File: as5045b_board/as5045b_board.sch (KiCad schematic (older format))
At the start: 10 parts

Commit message: QS
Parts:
- removed C?: 10uF, Capacitor_SMD:C_0603_1608Metric, symbol Device:C_Small
- removed C?: 0.1uF, Capacitor_SMD:C_0402_1005Metric, symbol Device:C_Small
- removed R? (x2): 10K, Resistor_SMD:R_0402_1005Metric, symbol Device:R_Small
- removed U? (x2): AS5045B, Package_SO:SSOP-16_5.3x6.2mm_P0.65mm, symbol Sensor_Magnetic:AS5045B
- added C1: 0.1uF, Capacitor_SMD:C_0402_1005Metric, symbol Device:C_Small
- added C3: 10uF, Capacitor_SMD:C_0603_1608Metric, symbol Device:C_Small
- added R1, R3, R5, R7: 2K2, Resistor_SMD:R_0402_1005Metric, symbol Device:R_Small
- added R10, R11, R12, R9: 10K, Resistor_SMD:R_0402_1005Metric, symbol Device:R_Small
- added R2, R4, R6, R8: 3K3, Resistor_SMD:R_0402_1005Metric, symbol Device:R_Small
- added U1, U2: AS5304, Package_SO:TSSOP-20_4.4x6.5mm_P0.65mm, symbol ams:AS5304
- gave numbers to parts that had none: 4
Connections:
- net labels added: +5V
- net labels removed: +3V3
- wire segments 30 -> 62
- no-connect marks 14 -> 0
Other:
- moved on the sheet: C2, C4, J1, J2

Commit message: Finished encoders, added XSHUT pullups
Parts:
- J1, J2: footprint Connector_PinHeader_1.00mm:PinHeader_1x04_P1.00mm_Vertical_SMD_Pin1Left -> connector_brd2brd:01x04_1.0x0.5mm_SMD
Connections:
- wire segments 62 -> 67
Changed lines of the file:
@@
 F 0 "J1" H 3700 3450 50  0000 C CNN
 F 1 "Conn_01x04" H 3700 3350 50  0000 C CNN
-F 2 "Connector_PinHeader_1.00mm:PinHeader_1x04_P1.00mm_Vertical_SMD_Pin1Left" H 3700 3100 50  0001 C CNN
+F 2 "connector_brd2brd:01x04_1.0x0.5mm_SMD" H 3700 3100 50  0001 C CNN
 F 3 "~" H 3700 3100 50  0001 C CNN
 	1    3700 3100
@@
 F 0 "J2" H 3700 4750 50  0000 C CNN
 F 1 "Conn_01x04" H 3700 4650 50  0000 C CNN
-F 2 "Connector_PinHeader_1.00mm:PinHeader_1x04_P1.00mm_Vertical_SMD_Pin1Left" H 3700 4400 50  0001 C CNN
+F 2 "connector_brd2brd:01x04_1.0x0.5mm_SMD" H 3700 4400 50  0001 C CNN
 F 3 "~" H 3700 4400 50  0001 C CNN
 	1    3700 4400
@@
 	1    0    0    -1
 $EndComp
-Connection ~ 5150 3300
 $Comp
 L Device:R_Small R9
@@
 	1    0    0    -1
 $EndComp
-Connection ~ 4900 3200
 $Comp
 L Device:R_Small R10
@@
 	1    0    0    -1
 $EndComp
-Connection ~ 4900 4500
 $Comp
 L Device:R_Small R12
@@
 	1    0    0    -1
 $EndComp
-Connection ~ 5150 4600
 $Comp
 L power:+5V #PWR0111
@@
 	3950 4600 3900 4600
 Connection ~ 4050 4800
-Wire Wire Line
-	4050 4600 5150 4600
-Wire Wire Line
-	4350 4500 4900 4500
 $Comp
 L power:GND #PWR0113
@@
 Connection ~ 4350 3400
 Wire Wire Line
-	4350 3200 4900 3200
-Wire Wire Line
-	4050 3300 5150 3300
-Wire Wire Line
 	3900 3100 4800 3100
 Wire Wire Line
@@
 	1    0    0    -1
 $EndComp
+Connection ~ 5150 3300
+Wire Wire Line
+	4050 3300 5150 3300
+Connection ~ 4900 3200
+Wire Wire Line
+	4350 3200 4900 3200
+Wire Wire Line
+	5150 4600 4550 4600
+Wire Wire Line
+	4550 4600 4550 4500
+Wire Wire Line
+	4550 4500 4350 4500
+Connection ~ 5150 4600
+Wire Wire Line
+	4650 4500 4650 4450
+Wire Wire Line
+	4650 4450 4050 4450
+Wire Wire Line
+	4050 4450 4050 4600
+Wire Wire Line
+	4650 4500 4900 4500
+Connection ~ 4900 4500
 $EndSCHEMATC

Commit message: Czyszczenie
Usunięto linie 5V oraz 2V8. Poprawiono symbol dla diody RGB
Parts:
- R10, R11, R12, R9: value 10K -> DNP
- U1, U2: symbol ams:AS5304 -> as5045b_board-rescue:AS5304-ams
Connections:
- wire segments 67 -> 72
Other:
- note added: "Note:\nPin 20 of AS5304 is connected manually\nto GND on PBC Layout Editor"
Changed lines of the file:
@@
 $EndComp
 $Comp
-L ams:AS5304 U1
+L as5045b_board-rescue:AS5304-ams U1
 U 1 1 5E66F302
 P 5750 3250
@@
 $EndComp
 $Comp
-L ams:AS5304 U2
+L as5045b_board-rescue:AS5304-ams U2
 U 1 1 5E66FC47
 P 5750 4550
@@
 P 5150 3200
 F 0 "R11" H 5209 3246 50  0000 L CNN
-F 1 "10K" H 5209 3155 50  0000 L CNN
+F 1 "DNP" H 5209 3155 50  0000 L CNN
 F 2 "Resistor_SMD:R_0402_1005Metric" H 5150 3200 50  0001 C CNN
 F 3 "~" H 5150 3200 50  0001 C CNN
@@
 P 4900 3100
 F 0 "R9" H 4959 3146 50  0000 L CNN
-F 1 "10K" H 4959 3055 50  0000 L CNN
+F 1 "DNP" H 4959 3055 50  0000 L CNN
 F 2 "Resistor_SMD:R_0402_1005Metric" H 4900 3100 50  0001 C CNN
 F 3 "~" H 4900 3100 50  0001 C CNN
@@
 P 4900 4400
 F 0 "R10" H 4959 4446 50  0000 L CNN
-F 1 "10K" H 4959 4355 50  0000 L CNN
+F 1 "DNP" H 4959 4355 50  0000 L CNN
 F 2 "Resistor_SMD:R_0402_1005Metric" H 4900 4400 50  0001 C CNN
 F 3 "~" H 4900 4400 50  0001 C CNN
@@
 P 5150 4500
 F 0 "R12" H 5209 4546 50  0000 L CNN
-F 1 "10K" H 5209 4455 50  0000 L CNN
+F 1 "DNP" H 5209 4455 50  0000 L CNN
 F 2 "Resistor_SMD:R_0402_1005Metric" H 5150 4500 50  0001 C CNN
 F 3 "~" H 5150 4500 50  0001 C CNN
@@
 $EndComp
 Connection ~ 5150 3300
-Wire Wire Line
-	4050 3300 5150 3300
 Connection ~ 4900 3200
 Wire Wire Line
-	4350 3200 4900 3200
+	4350 3200 4550 3200
+Connection ~ 5150 4600
+Connection ~ 4900 4500
+Wire Wire Line
+	4650 4500 4900 4500
+Wire Wire Line
+	4550 4500 4350 4500
 Wire Wire Line
 	5150 4600 4550 4600
@@
 	4550 4600 4550 4500
 Wire Wire Line
-	4550 4500 4350 4500
-Connection ~ 5150 4600
+	4050 4450 4050 4600
 Wire Wire Line
 	4650 4500 4650 4450
@@
 	4650 4450 4050 4450
 Wire Wire Line
-	4050 4450 4050 4600
-Wire Wire Line
-	4650 4500 4900 4500
-Connection ~ 4900 4500
+	4050 3300 4050 3150
+Wire Wire Line
+	4050 3150 4650 3150
+Wire Wire Line
+	4650 3150 4650 3200
+Wire Wire Line
+	4650 3200 4900 3200
+Wire Wire Line
+	4550 3300 4550 3200
+Wire Wire Line
+	4550 3300 5150 3300
+Wire Notes Line
+	4600 2050 6250 2050
+Wire Notes Line
+	6250 2050 6250 2400
+Wire Notes Line
+	6250 2400 4600 2400
+Wire Notes Line
+	4600 2400 4600 2050
+Text Notes 4600 2350 0    50   ~ 0
+Note:\nPin 20 of AS5304 is connected manually\nto GND on PBC Layout Editor
 $EndSCHEMATC

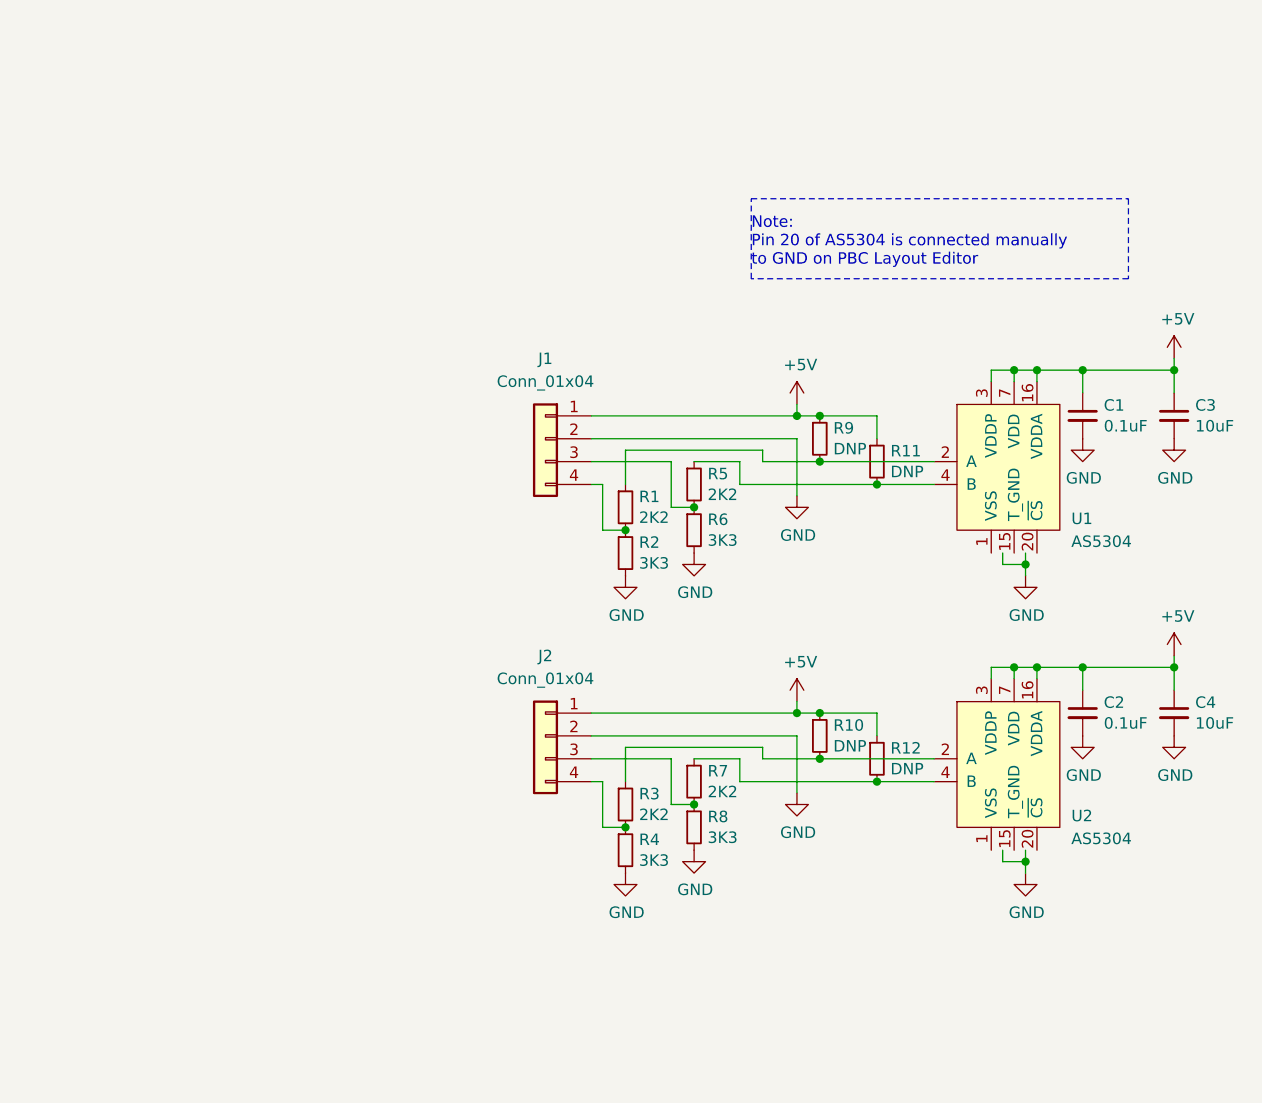
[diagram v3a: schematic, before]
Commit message: Updated BT module connection, 3D models and wiring.
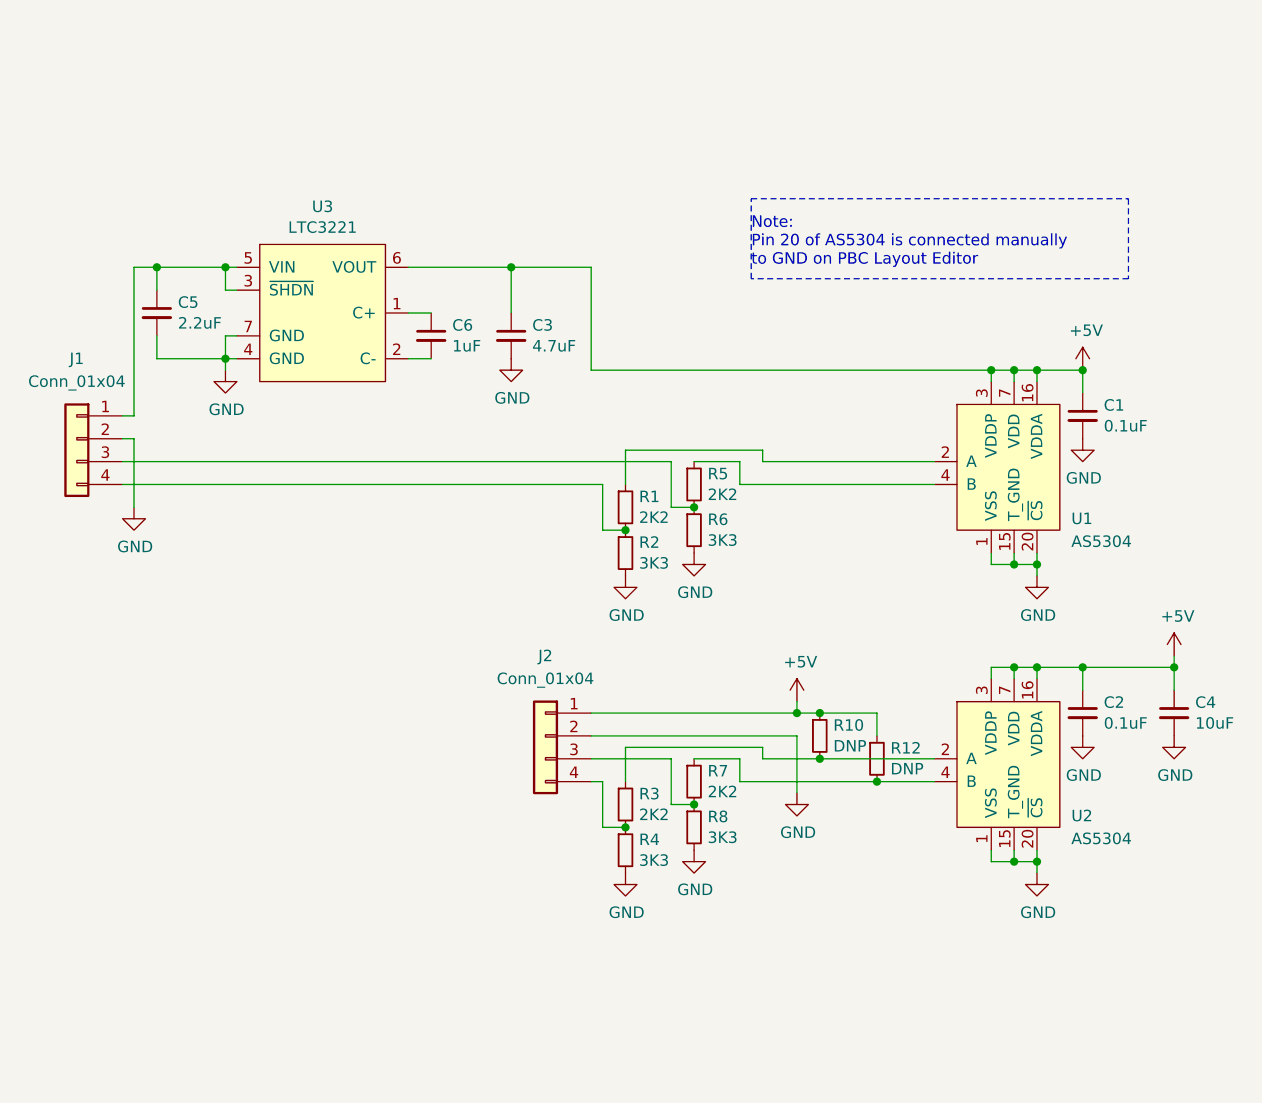
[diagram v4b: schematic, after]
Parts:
- removed R11, R9: DNP, Resistor_SMD:R_0402_1005Metric, symbol Device:R_Small
- added C5: 2.2uF, Capacitor_SMD:C_0603_1608Metric, symbol Device:C_Small
- added C6: 1uF, Capacitor_SMD:C_0402_1005Metric, symbol Device:C_Small
- added U3: LTC3221, Package_DFN_QFN:DFN-6-1EP_2x2mm_P0.5mm_EP0.61x1.42mm, symbol synermycha-electronics:LTC3221
- C3: value 10uF -> 4.7uF
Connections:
- wire segments 72 -> 87
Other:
- moved on the sheet: C3, J1

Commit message: Encoders update
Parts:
- removed C4: 10uF, Capacitor_SMD:C_0603_1608Metric, symbol Device:C_Small
- removed R10, R12: DNP, Resistor_SMD:R_0402_1005Metric, symbol Device:R_Small
- added C7: 2.2uF, Capacitor_SMD:C_0603_1608Metric, symbol Device:C_Small
- added C8: 1uF, Capacitor_SMD:C_0402_1005Metric, symbol Device:C_Small
- added C9: 4.7uF, Capacitor_SMD:C_0603_1608Metric, symbol Device:C_Small
- added U4: LTC3221, Package_DFN_QFN:DFN-6-1EP_2x2mm_P0.5mm_EP0.61x1.42mm, symbol synermycha-electronics:LTC3221
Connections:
- net +5V: now also C9.1, U4.6 (VOUT); no longer J2.1 (Pin_1)
- net GND: now also C7.2, C9.2, U4.4 (GND), U4.7 (GND)
- net at R5.2, R6.1: now also J1.4 (Pin_4); no longer J1.3 (Pin_3)
- net at R1.2, R2.1: now also J1.3 (Pin_3); no longer J1.4 (Pin_4)
- new net: C7.1, J2.1 (Pin_1), U4.3 (~SHDN), U4.5 (VIN)
- new net: C8.1, U4.1 (C+)
- new net: C8.2, U4.2 (C-)
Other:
- moved on the sheet: C2, J2, R3, R4, R7, R8, U2
